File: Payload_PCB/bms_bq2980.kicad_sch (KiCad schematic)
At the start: 12 parts, among them Q1 Q_NMOS_DGS, Q12 Q_NMOS_DGS, U12 BQ298000RUGR

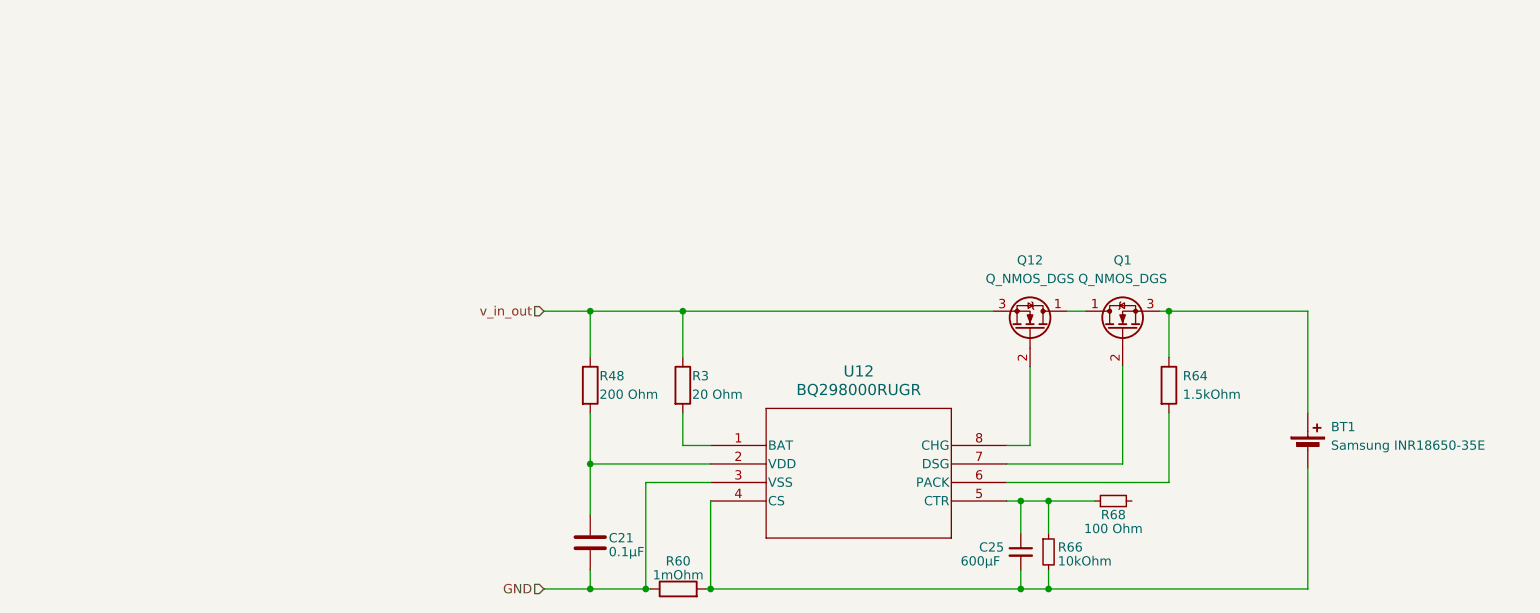
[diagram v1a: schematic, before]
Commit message: Added heating pad, adjustment of page sizes
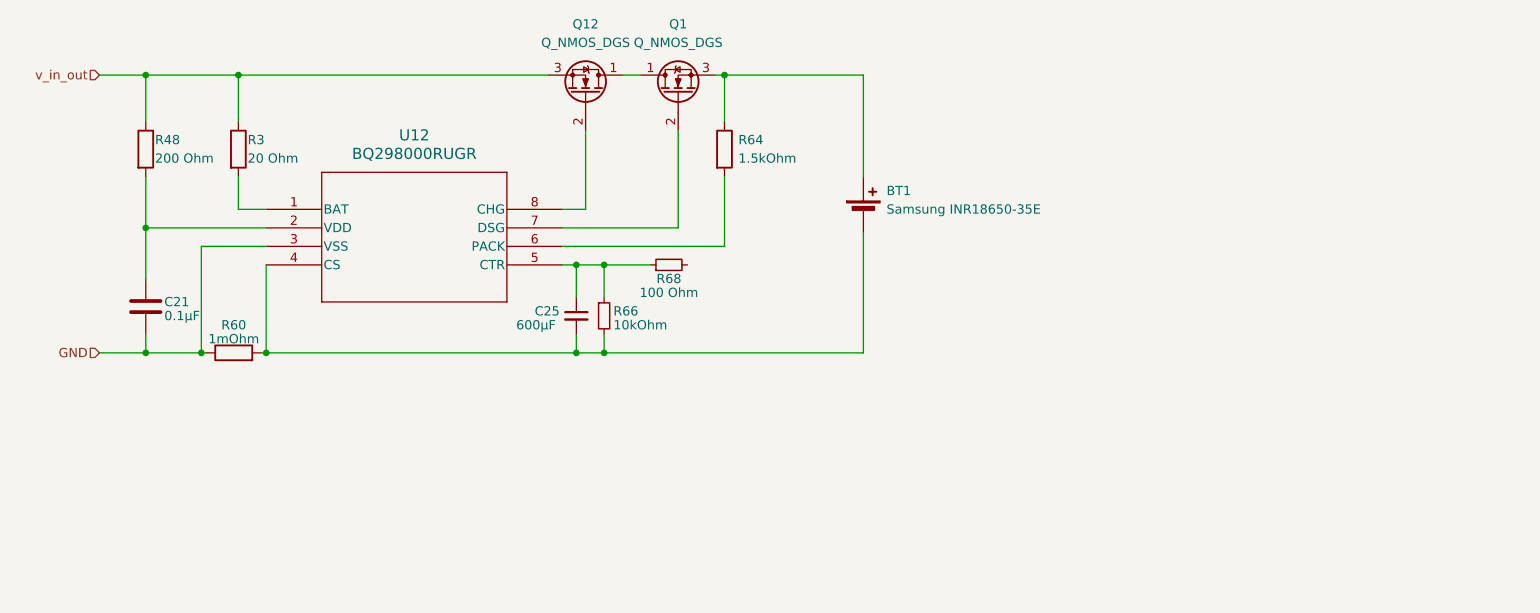
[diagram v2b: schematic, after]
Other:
- moved on the sheet: BT1, C21, C25, Q1, Q12, R3, R48, R60, R64, R66, R68, U12

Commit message: Added some actual parts
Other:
- company: (none) -> SpaceTeam Aachen
- title: (none) -> Battery and BMS
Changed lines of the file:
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@@
 (kicad_sch (version 20230121) (generator eeschema)
   (paper "A5")
+  (title_block
+    (title "Battery and BMS")
+    (company "SpaceTeam Aachen")
+  )
   (junction (at 66.04 49.53) (diameter 0) (color 0 0 0 0)
   )

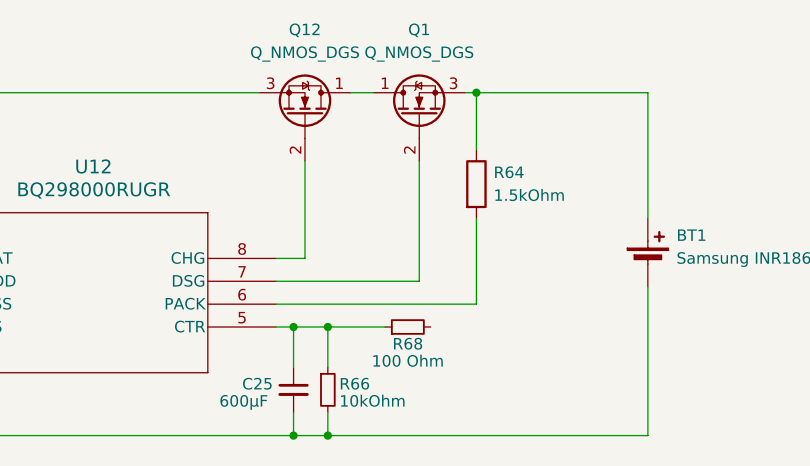
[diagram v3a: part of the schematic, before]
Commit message: Change to actual real parts
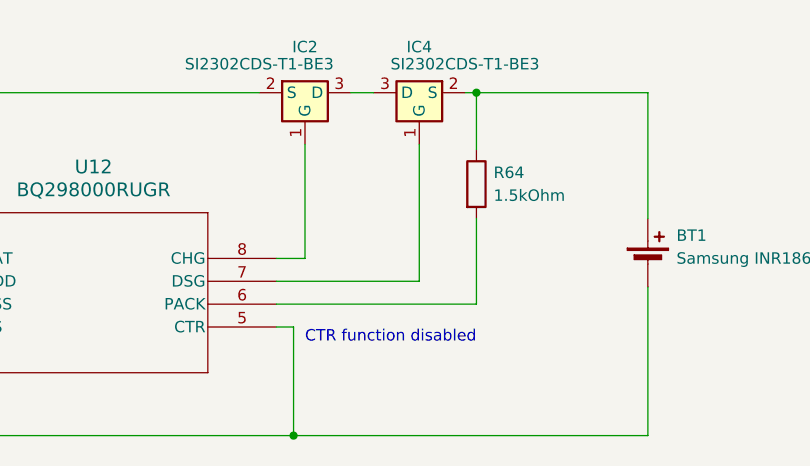
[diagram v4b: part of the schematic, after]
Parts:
- removed C25: 600µF, symbol Device:C_Small
- removed Q1, Q12: Q_NMOS_DGS, symbol Device:Q_NMOS_DGS
- removed R66: 10kOhm, symbol Device:R_Small
- removed R68: 100 Ohm, symbol Device:R_Small
- added IC2, IC4: SI2302CDS-T1-BE3, SOT95P237X112-3N, symbol SI2302CDS-T1-BE3:SI2302CDS-T1-BE3
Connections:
- net v_in_out: now also IC2.2 (S)
- net at BT1.1 (+), R64.1: now also IC4.2 (S)
- net at U12.8 (CHG): now also IC2.1 (G)
- net at U12.5 (CTR): now also BT1.2 (-), R60.2, U12.4 (CS)
- net at U12.7 (DSG): now also IC4.1 (G)
- new net: IC2.3 (D), IC4.3 (D)
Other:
- note added: "CTR function disabled"

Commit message: some new parts
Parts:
- BT1: footprint (none) -> footprints:SamsungINR18650-35E_U
- IC2, IC4: footprint SOT95P237X112-3N -> footprints:SOT95P237X112-3N
- U12: footprint RUG8_TEX -> footprints:ADS7056IRUGR
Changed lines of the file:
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@@
       (effects (font (size 1.27 1.27)))
     )
-    (property "Footprint" "SOT95P237X112-3N" (at 125.095 144.45 0)
+    (property "Footprint" "footprints:SOT95P237X112-3N" (at 125.095 144.45 0)
       (effects (font (size 1.27 1.27)) (justify left top) hide)
     )
@@
       (effects (font (size 1.27 1.27)))
     )
-    (property "Footprint" "SOT95P237X112-3N" (at 114.935 144.45 0)
+    (property "Footprint" "footprints:SOT95P237X112-3N" (at 114.935 144.45 0)
       (effects (font (size 1.27 1.27)) (justify left top) hide)
     )
@@
       (effects (font (size 1.524 1.524)))
     )
-    (property "Footprint" "RUG8_TEX" (at 69.85 67.945 0)
+    (property "Footprint" "footprints:ADS7056IRUGR" (at 69.85 67.945 0)
       (effects (font (size 1.27 1.27) italic) hide)
     )
@@
       (effects (font (size 1.27 1.27)) (justify left))
     )
-    (property "Footprint" "" (at 151.765 67.056 90)
+    (property "Footprint" "footprints:SamsungINR18650-35E_U" (at 151.765 67.056 90)
       (effects (font (size 1.27 1.27)) hide)
     )
